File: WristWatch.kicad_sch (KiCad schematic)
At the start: 60 parts

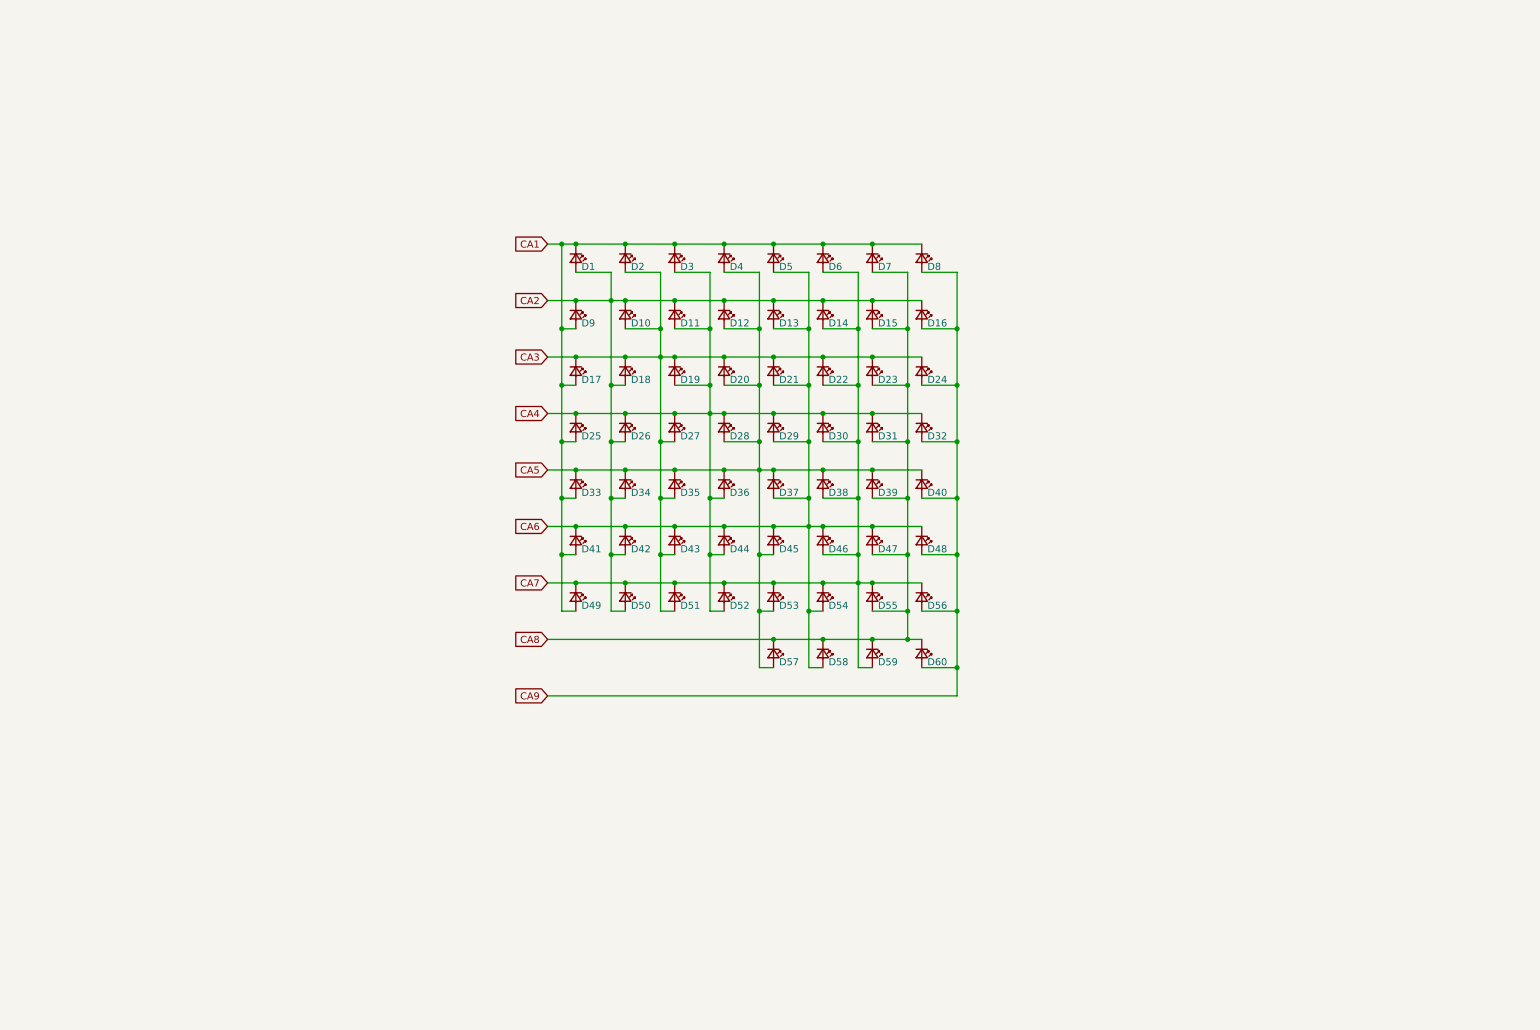
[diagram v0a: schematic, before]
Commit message: Unknown progress. Pending twisted charlieplex experiments
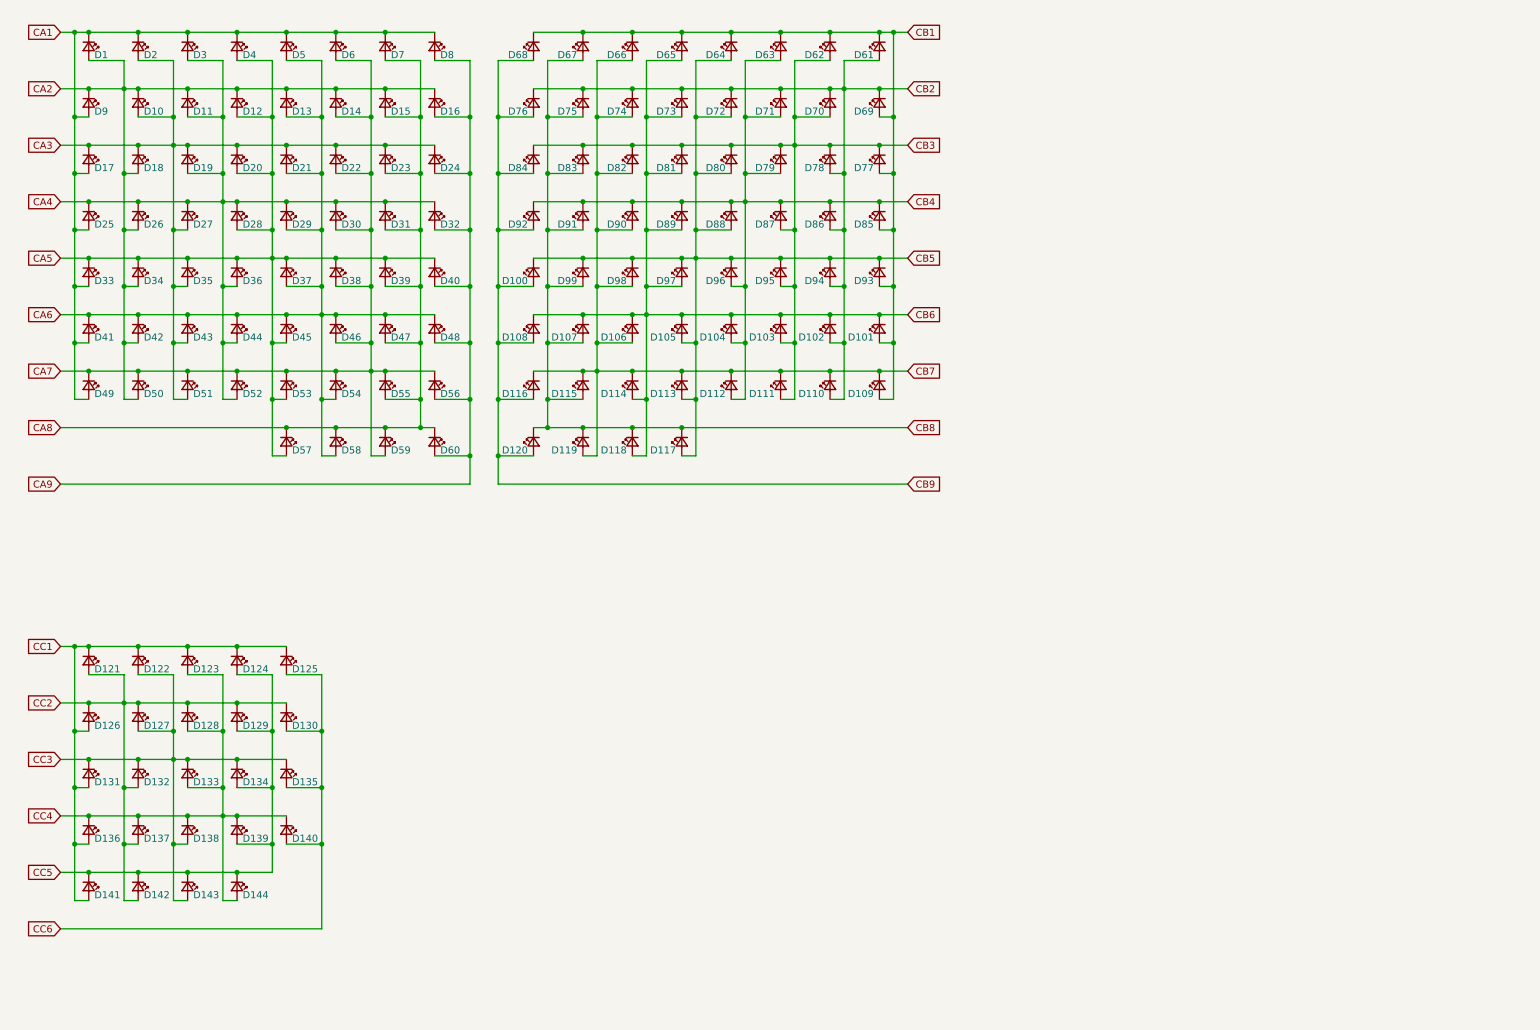
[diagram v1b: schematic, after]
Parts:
- added D100, D101, D102, D103, D104, D105, D106, D107, D108, D109, D110, D111, D112, D113, D114, D115, D116, D117, D118, D119, D120, D121, D122, D123, D124, D125, D126, D127, D128, D129, D130, D131, D132, D133, D134, D135, D136, D137, D138, D139, D140, D141, D142, D143, D144, D61, D62, D63, D64, D65, D66, D67, D68, D69, D70, D71, D72, D73, D74, D75, D76, D77, D78, D79, D80, D81, D82, D83, D84, D85, D86, D87, D88, D89, D90, D91, D92, D93, D94, D95, D96, D97, D98, D99: LED_Small, LED_SMD:LED_0603_1608Metric, symbol Device:LED_Small
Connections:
- new net CB1: D101.2 (A), D109.2 (A), D61.1 (K), D62.1 (K), D63.1 (K), D64.1 (K), D65.1 (K), D66.1 (K), D67.1 (K), D68.1 (K), D69.2 (A), D77.2 (A), D85.2 (A), D93.2 (A)
- new net CB2: D102.2 (A), D110.2 (A), D61.2 (A), D69.1 (K), D70.1 (K), D71.1 (K), D72.1 (K), D73.1 (K), D74.1 (K), D75.1 (K), D76.1 (K), D78.2 (A), D86.2 (A), D94.2 (A)
- new net CB3: D103.2 (A), D111.2 (A), D62.2 (A), D70.2 (A), D77.1 (K), D78.1 (K), D79.1 (K), D80.1 (K), D81.1 (K), D82.1 (K), D83.1 (K), D84.1 (K), D87.2 (A), D95.2 (A)
- new net CB4: D104.2 (A), D112.2 (A), D63.2 (A), D71.2 (A), D79.2 (A), D85.1 (K), D86.1 (K), D87.1 (K), D88.1 (K), D89.1 (K), D90.1 (K), D91.1 (K), D92.1 (K), D96.2 (A)
- new net CB5: D100.1 (K), D105.2 (A), D113.2 (A), D117.2 (A), D64.2 (A), D72.2 (A), D80.2 (A), D88.2 (A), D93.1 (K), D94.1 (K), D95.1 (K), D96.1 (K), D97.1 (K), D98.1 (K), D99.1 (K)
- new net CB6: D101.1 (K), D102.1 (K), D103.1 (K), D104.1 (K), D105.1 (K), D106.1 (K), D107.1 (K), D108.1 (K), D114.2 (A), D118.2 (A), D65.2 (A), D73.2 (A), D81.2 (A), D89.2 (A), D97.2 (A)
- new net CB7: D106.2 (A), D109.1 (K), D110.1 (K), D111.1 (K), D112.1 (K), D113.1 (K), D114.1 (K), D115.1 (K), D116.1 (K), D119.2 (A), D66.2 (A), D74.2 (A), D82.2 (A), D90.2 (A), D98.2 (A)
- new net CB8: D107.2 (A), D115.2 (A), D117.1 (K), D118.1 (K), D119.1 (K), D120.1 (K), D67.2 (A), D75.2 (A), D83.2 (A), D91.2 (A), D99.2 (A)
- new net CB9: D100.2 (A), D108.2 (A), D116.2 (A), D120.2 (A), D68.2 (A), D76.2 (A), D84.2 (A), D92.2 (A)
- new net CC1: D121.1 (K), D122.1 (K), D123.1 (K), D124.1 (K), D125.1 (K), D126.2 (A), D131.2 (A), D136.2 (A), D141.2 (A)
- new net CC2: D121.2 (A), D126.1 (K), D127.1 (K), D128.1 (K), D129.1 (K), D130.1 (K), D132.2 (A), D137.2 (A), D142.2 (A)
- new net CC3: D122.2 (A), D127.2 (A), D131.1 (K), D132.1 (K), D133.1 (K), D134.1 (K), D135.1 (K), D138.2 (A), D143.2 (A)
- new net CC4: D123.2 (A), D128.2 (A), D133.2 (A), D136.1 (K), D137.1 (K), D138.1 (K), D139.1 (K), D140.1 (K), D144.2 (A)
- new net CC5: D124.2 (A), D129.2 (A), D134.2 (A), D139.2 (A), D141.1 (K), D142.1 (K), D143.1 (K), D144.1 (K)
- new net CC6: D125.2 (A), D130.2 (A), D135.2 (A), D140.2 (A)
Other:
- moved on the sheet: D1, D10, D11, D12, D13, D14, D15, D16, D17, D18, D19, D2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

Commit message: Start layout. MCU close, LEDs correct, pending esp32
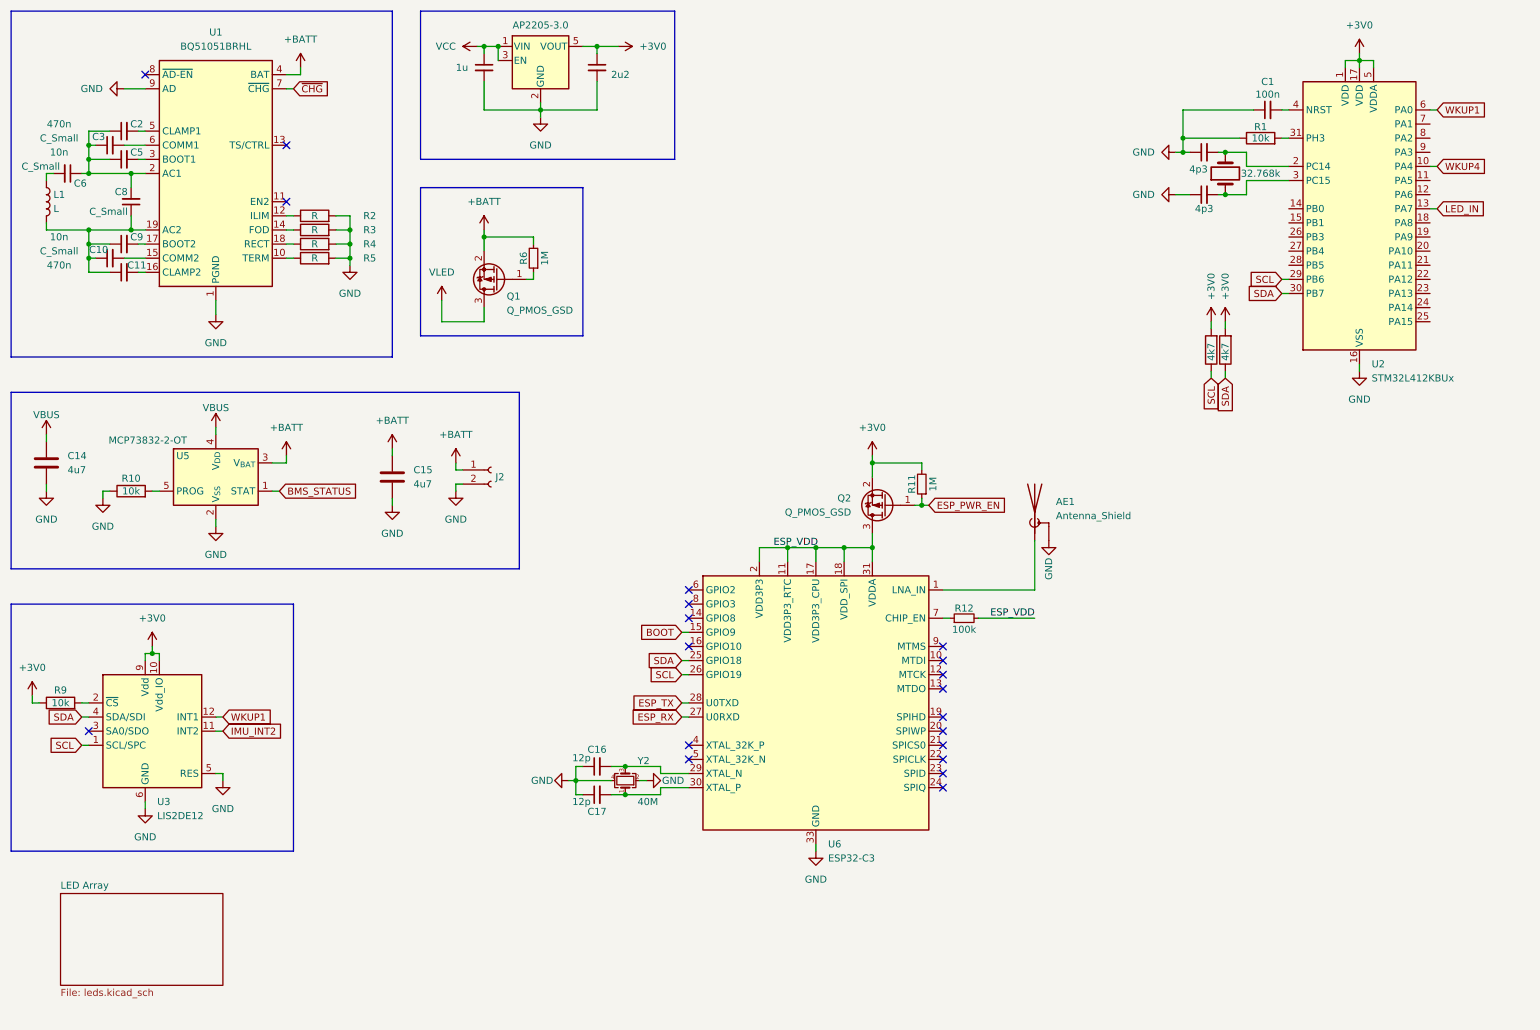
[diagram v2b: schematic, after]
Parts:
- removed D1, D10, D100, D101, D102, D103, D104, D105, D106, D107, D108, D109, D11, D110, D111, D112, D113, D114, D115, D116, D117, D118, D119, D12, D120, D121, D122, D123, D124, D125, D126, D127, D128, D129, D13, D130, D131, D132, D133, D134, D135, D136, D137, D138, D139, D14, D140, D141, D142, D143, D144, D15, D16, D17, D18, D19, D2, D20, D21, D22, D23, D24, D25, D26, D27, D28, D29, D3, D30, D31, D32, D33, D34, D35, D36, D37, D38, D39, D4, D40, D41, D42, D43, D44, D45, D46, D47, D48, D49, D5, D50, D51, D52, D53, D54, D55, D56, D57, D58, D59, D6, D60, D61, D62, D63, D64, D65, D66, D67, D68, D69, D7, D70, D71, D72, D73, D74, D75, D76, D77, D78, D79, D8, D80, D81, D82, D83, D84, D85, D86, D87, D88, D89, D9, D90, D91, D92, D93, D94, D95, D96, D97, D98, D99: LED_Small, LED_SMD:LED_0603_1608Metric, symbol Device:LED_Small
- added AE1: Antenna_Shield, Antenna_SMD:C209892, symbol Device:Antenna_Shield
- added C1: 100n, Capacitor_SMD:C_0402_1005Metric, symbol Device:C_Small
- added C10, C3, C6, C8: C_Small, Capacitor_SMD:C_0402_1005Metric, symbol Device:C_Small
- added C11, C2: 470n, Capacitor_SMD:C_0402_1005Metric, symbol Device:C_Small
- added C12: 1u, Capacitor_SMD:C_0402_1005Metric, symbol Device:C_Small
- added C13: 2u2, Capacitor_SMD:C_0402_1005Metric, symbol Device:C_Small
- added C14, C15: 4u7, Capacitor_SMD:C_0402_1005Metric, symbol Device:C
- added C16, C17: 12p, Capacitor_SMD:C_0402_1005Metric, symbol Device:C_Small
- added C4, C7: 4p3, Capacitor_SMD:C_0402_1005Metric, symbol Device:C_Small
- added C5, C9: 10n, Capacitor_SMD:C_0402_1005Metric, symbol Device:C_Small
- added J2: Conn_01x02_Socket, Connector_PinHeader_2.00mm:PinHeader_1x02_P2.00mm_Vertical, symbol Connector:Conn_01x02_Socket
- added L1: L, Connector_PinHeader_1.27mm:PinHeader_1x02_P1.27mm_Vertical, symbol Device:L
- added Q1, Q2: Q_PMOS_GSD, Package_TO_SOT_SMD:SOT-523, symbol Device:Q_PMOS_GSD
- added R1, R10, R9: 10k, Resistor_SMD:R_0402_1005Metric, symbol Device:R
- added R11, R6: 1M, Resistor_SMD:R_0402_1005Metric, symbol Device:R_Small
- added R12: 100k, Resistor_SMD:R_0402_1005Metric, symbol Device:R_Small
- added R2, R3, R4, R5: R, Resistor_SMD:R_0402_1005Metric, symbol Device:R
- added R7, R8: 4k7, Resistor_SMD:R_0402_1005Metric, symbol Device:R
- added U1: BQ51051BRHL, Package_DFN_QFN:Texas_VQFN-RHL-20, symbol Battery_Management:BQ51051BRHL
- added U2: STM32L412KBUx, Package_DFN_QFN:QFN-32-1EP_5x5mm_P0.5mm_EP3.45x3.45mm, symbol MCU_ST_STM32L4:STM32L412KBUx
- added U3: LIS2DE12, Package_LGA:LGA-12_2x2mm_P0.5mm, symbol Sensor_Motion:LIS2DE12
- added U4: AP2205-3.0, Package_TO_SOT_SMD:SOT-23-5, symbol Regulator_Linear:AP2127K-3.0
- added U5: MCP73832-2-OT, Package_TO_SOT_SMD:SOT-23-5, symbol Battery_Management:MCP73832-2-OT
- added U6: ESP32-C3, Package_DFN_QFN:QFN-32-1EP_5x5mm_P0.5mm_EP3.7x3.7mm, symbol MCU_Espressif:ESP32-C3
- added Y1: 32.768k, Crystal:Crystal_SMD_3215-2Pin_3.2x1.5mm, symbol Device:Crystal
- added Y2: 40M, SMD_Crystal:Crystal_SMD_1612_4P, symbol Device:Crystal_GND24_Small
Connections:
- new net: R5.1, U1.10 (TERM)
- new net: R9.2, U3.2 (~{CS})
- new net: R3.1, U1.14 (FOD)
- new net: C7.2, U2.3 (PC15), Y1.1
- new net: C17.2, U6.30 (XTAL_P), Y2.1
- new net: Q1.1 (G), R6.1
- new net: C2.1, C3.1, C5.1, C6.1, C8.2, U1.2 (AC1)
- new net: C2.2, U1.5 (CLAMP1)
- new net: C4.2, U2.2 (PC14), Y1.2
- new net: R4.1, U1.18 (RECT)
- new net: R10.2, U5.5 (PROG)
- new net: C3.2, U1.6 (COMM1)
- new net: C16.2, U6.29 (XTAL_N), Y2.3
- new net: R12.1, U6.7 (CHIP_EN)
- new net: C10.1, C11.1, C8.1, C9.1, L1.2, U1.19 (AC2)
- new net: C11.2, U1.16 (CLAMP2)
- new net: AE1.1 (A), U6.1 (LNA_IN)
- new net: C1.2, U2.4 (NRST)
- new net: C5.2, U1.3 (BOOT1)
- new net: C10.2, U1.15 (COMM2)
- new net: R2.1, U1.12 (ILIM)
- new net: C9.2, U1.17 (BOOT2)
- new net: C6.2, L1.1
- new net: R1.2, U2.31 (PH3)
- new net +3V0: C13.1, Q2.2 (S), R11.2, R7.2, R8.2, R9.1, U2.1 (VDD), U2.17 (VDD), U2.5 (VDDA), U3.10 (Vdd_IO), U3.9 (Vdd), U4.5 (VOUT)
- new net +BATT: C15.1, J2.1 (Pin_1), Q1.2 (S), R6.2, U1.4 (BAT), U5.3 (V_{BAT})
- new net BMS_STATUS: U5.1 (STAT)
- new net BOOT: U6.15 (GPIO9)
- new net ESP_PWR_EN: Q2.1 (G), R11.1
- new net ESP_RX: U6.27 (U0RXD)
- new net ESP_TX: U6.28 (U0TXD)
- new net ESP_VDD: Q2.3 (D), R12.2, U6.11 (VDD3P3_RTC), U6.17 (VDD3P3_CPU), U6.18 (VDD_SPI), U6.2 (VDD3P3), U6.3 (VDD3P3), U6.31 (VDDA), U6.32 (VDDA)
- new net GND: AE1.2 (Shield), C1.1, C12.2, C13.2, C14.2, C15.2, C16.1, C17.1, C4.1, C7.1, J2.2 (Pin_2), R1.1, R10.1, R2.2, R3.2, R4.2, R5.2, U1.1 (PGND), U1.20 (PGND), U1.21 (PGND), U1.9 (AD), U2.16 (VSS), U2.32 (VSS), U2.33 (VSS), U3.5 (RES), U3.6 (GND), U3.7 (GND), U3.8 (GND), U4.2 (GND), U5.2 (V_{SS}), U6.33 (GND), Y2.2, Y2.4
- new net IMU_INT2: U3.11 (INT2)
- new net LED_IN: U2.13 (PA7)
- new net SCL: R7.1, U2.29 (PB6), U3.1 (SCL/SPC), U6.26 (GPIO19)
- new net SDA: R8.1, U2.30 (PB7), U3.4 (SDA/SDI), U6.25 (GPIO18)
- new net VBUS: C14.1, U5.4 (V_{DD})
- new net VCC: C12.1, U4.1 (VIN), U4.3 (EN)
- new net VLED: Q1.3 (D)
- new net WKUP1: U2.6 (PA0), U3.12 (INT1)
- new net WKUP4: U2.10 (PA4)
- new net ~{CHG}: U1.7 (~{CHG})
- no-connect marks 0 -> 20
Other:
- added sheet LED Array (leds.kicad_sch)

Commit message: This board is actually stupid. Moving on. Dual MCU architecture felt cool. It was in fact, overly complicated. Finally got the STM32F401 RTC to work. Fighting the L412 though.
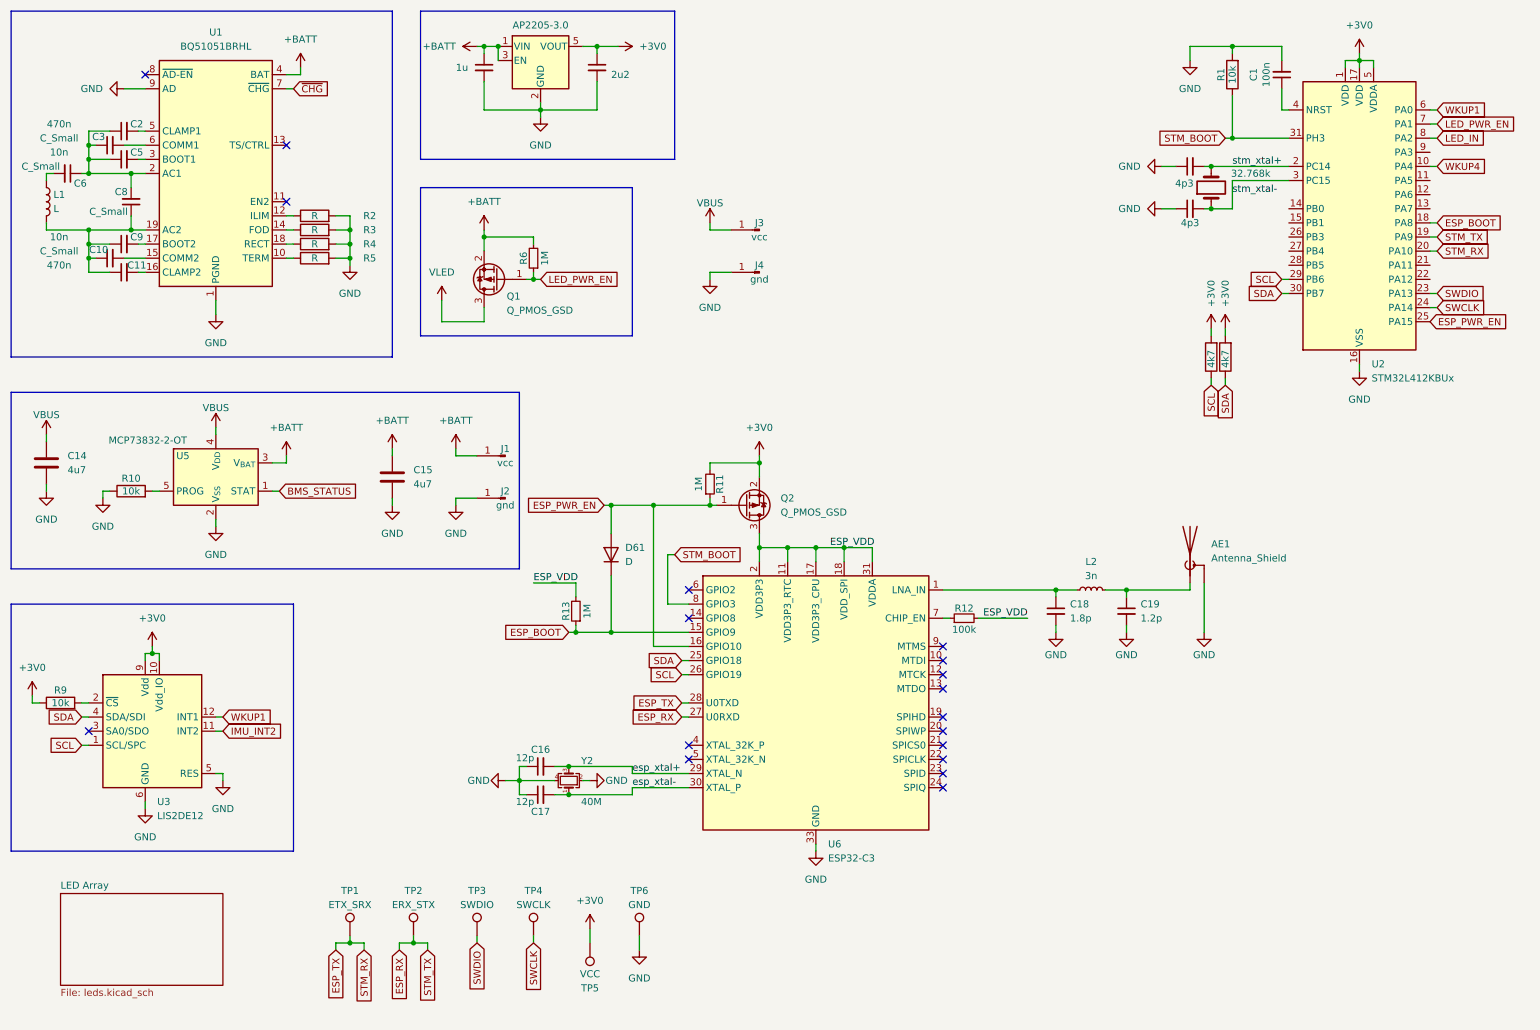
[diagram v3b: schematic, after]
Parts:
- removed J2: Conn_01x02_Socket, Connector_PinHeader_2.00mm:PinHeader_1x02_P2.00mm_Vertical, symbol Connector:Conn_01x02_Socket
- added C18: 1.8p, Capacitor_SMD:C_0402_1005Metric, symbol Device:C_Small
- added C19: 1.2p, Capacitor_SMD:C_0402_1005Metric, symbol Device:C_Small
- added D61: D, Diode_SMD:D_SOD-523, symbol Device:D
- added J1, J3: vcc, TestPoint:TestPoint_Pad_D1.0mm, symbol Connector:Conn_01x01_Pin
- added J2, J4: gnd, TestPoint:TestPoint_Pad_D1.0mm, symbol Connector:Conn_01x01_Pin
- added L2: 3n, Inductor_SMD:L_0402_1005Metric, symbol Device:L_Small
- added R13: 1M, Resistor_SMD:R_0402_1005Metric, symbol Device:R_Small
- added TP1: ETX_SRX, TestPoint:TestPoint_Pad_D1.5mm, symbol Connector:TestPoint
- added TP2: ERX_STX, TestPoint:TestPoint_Pad_D1.5mm, symbol Connector:TestPoint
- added TP3: SWDIO, TestPoint:TestPoint_Pad_D1.5mm, symbol Connector:TestPoint
- added TP4: SWCLK, TestPoint:TestPoint_Pad_D1.5mm, symbol Connector:TestPoint
- added TP5: VCC, TestPoint:TestPoint_Pad_D1.5mm, symbol Connector:TestPoint
- added TP6: GND, TestPoint:TestPoint_Pad_D1.5mm, symbol Connector:TestPoint
- Y2: footprint SMD_Crystal:Crystal_SMD_1612_4P -> Crystal:Crystal_SMD_2520-4Pin_2.5x2.0mm
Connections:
- net BOOT is gone; now on net ESP_BOOT: U6.15 (GPIO9)
- net VCC is gone; now on net +BATT: C12.1, U4.1 (VIN), U4.3 (EN)
- net +3V0: now also TP5.1
- net +BATT: now also J1.1 (Pin_1)
- net ESP_PWR_EN: now also U2.25 (PA15), U6.16 (GPIO10), D61.2 (A)
- net ESP_RX: now also U2.19 (PA9), TP2.1
- net ESP_TX: now also U2.20 (PA10), TP1.1
- net ESP_VDD: now also R13.2
- net GND: now also C1.2, R1.2, C18.2, C19.2, J2.1 (Pin_1), J4.1 (Pin_1), TP6.1; no longer C1.1, R1.1
- net LED_IN: now also U2.8 (PA2); no longer U2.13 (PA7)
- net VBUS: now also J3.1 (Pin_1)
- net stm_xtal-: now reaches C7.2, U2.3 (PC15), Y1.1
- net esp_xtal-: now reaches C17.2, U6.30 (XTAL_P), Y2.1
- net LED_PWR_EN: now reaches Q1.1 (G), R6.1
- net LED_PWR_EN: now also U2.7 (PA1)
- net stm_xtal+: now reaches C4.2, U2.2 (PC14), Y1.2
- net esp_xtal+: now reaches C16.2, U6.29 (XTAL_N), Y2.3
- net at U6.1 (LNA_IN): now also C18.1, L2.1; no longer AE1.1 (A)
- net at U2.4 (NRST): now also C1.1; no longer C1.2
- net STM_BOOT: now reaches U6.8 (GPIO3)
- net STM_BOOT: now also R1.1, U2.31 (PH3)
- net ESP_BOOT: now reaches U2.18 (PA8)
- net ESP_BOOT: now also D61.1 (K), R13.1
- net SWDIO: now reaches U2.23 (PA13)
- net SWDIO: now also TP3.1
- net SWCLK: now reaches U2.24 (PA14)
- net SWCLK: now also TP4.1
- new net: AE1.1 (A), C19.1, L2.2
- no-connect marks 20 -> 18
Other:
- moved on the sheet: AE1, C1, C16, C17, Q2, R1, R11, Y2
